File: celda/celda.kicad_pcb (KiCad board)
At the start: 4 copper layers, 119.6 x 48.1 mm, 87 parts, among them Q1 MMBT2222A, Q2 MMBT2222A, Q3 MMBT2222A, Q4 MMBT2222A, Q5 MMBT2222A, Q6 MMBT2222A, Q7 MMBT2222A, Q8 MMBT2222A, U1 LM339D, U10 BTS50010-1TAD, U11 BTS50010-1TAD, U2 74HC132D, U3 BTS50010-1TAD, U8 BTS50010-1TAD, U9 74HC132D

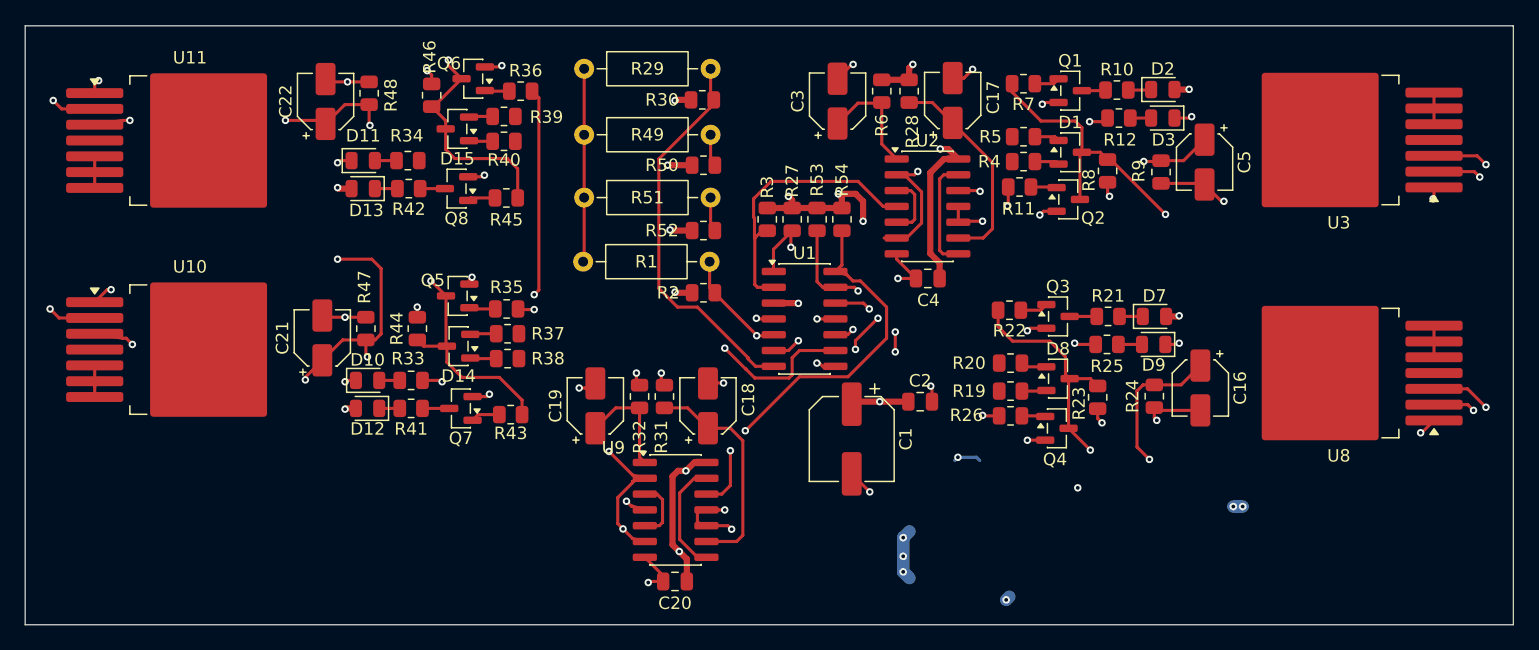
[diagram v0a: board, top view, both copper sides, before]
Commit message: Rediseña la celda dorada a doble cara y unifica el UUID raíz
Los componentes de control pasan a ambas caras (BTS y resistencias
THT DNP en F.Cu; LM339, 74HC132, transistores, BAT54C y la mayoría de
resistencias en B.Cu). La zona de huellas baja de 112,8 x 43,7 mm a
unos 82 x 35 mm (alrededor de un 41 % menos de área). Se cierran los
puentes de salida de los BTS y la red FALLA4.

El UUID de la hoja raíz, el del proyecto y las rutas de las huellas
quedan iguales, lo que elimina los 28 avisos de paridad del DRC.
El netlist es idéntico al anterior.

Pendiente en la celda: tiras de +12 V (7 conexiones abiertas), ajustar
el contorno Edge.Cuts al nuevo tamaño y la serigrafía de 0,7 mm.
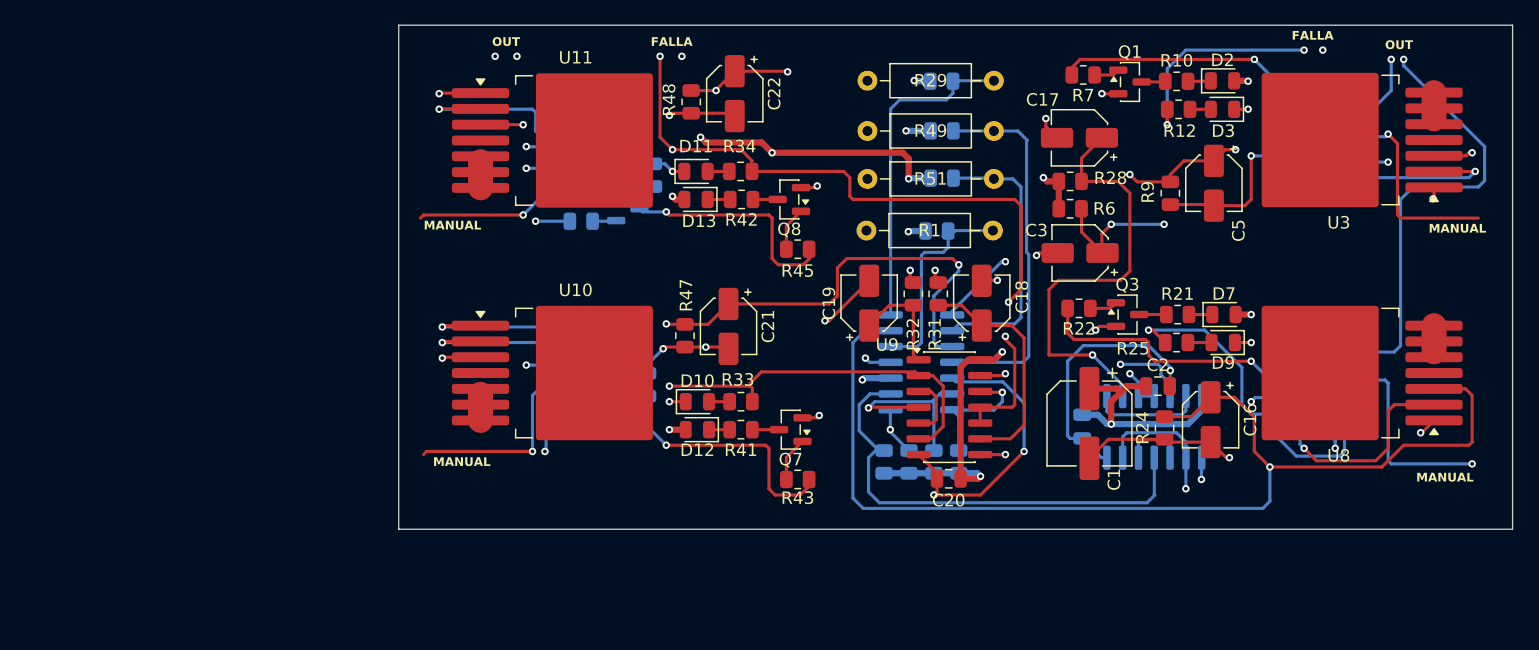
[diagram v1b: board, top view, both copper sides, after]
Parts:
- C4, D1, D14, D15, D8, Q2, Q4, Q5, Q6, R11, R19, R2, R20, R23, R26, R27, R3, R30, R35, R36, R37, R38, R39, R4, R40, R44, R46, R5, R50, R52, R53, R54, R8, U1, U2: moved to B.Cu
- moved C22 32.9 mm to (-110.5, 33.0), turned to -90 degrees
- moved C21 32.7 mm to (-111.0, 51.7), turned to -90 degrees
- moved U10 31.1 mm to (-123.3, 55.5)
- moved U11 31.0 mm to (-123.3, 36.8)
- moved R26 27.9 mm to (-60.4, 58.0), turned to 0 degrees
- moved R19 27.9 mm to (-60.4, 56.0), turned to 180 degrees
- moved R20 27.9 mm to (-60.4, 53.8), turned to 0 degrees
- moved R11 27.3 mm to (-60.3, 38.5), turned to 0 degrees
- moved D11 26.8 mm to (-113.6, 39.2)
- moved D13 26.8 mm to (-113.6, 41.5)
- moved Q8 26.8 mm to (-106.1, 41.5)
- moved R42 26.8 mm to (-110.0, 41.5)
- moved R34 26.8 mm to (-110.0, 39.2)
- moved R4 26.7 mm to (-60.7, 36.5), turned to 180 degrees
- moved R5 26.7 mm to (-60.7, 34.5), turned to 0 degrees
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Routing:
- net GND: track 86.6 -> 141.6 mm, vias 41 -> 27
- net /FALLA1: track 36.4 -> 90.5 mm, vias 3 -> 4
- net /ESP32_OUT3: track 0.00 -> 47.0 mm, vias 0 -> 2
- net /FALLA2: track 29.5 -> 72.2 mm
- net /FALLA3: track 35.9 -> 74.8 mm, vias 4 -> 3
- net Net-(U10-IS): track 96.6 -> 58.2 mm, vias 7 -> 3
- net /ESP32_OUT2: track 0.00 -> 34.3 mm, vias 0 -> 1
- net Net-(C3-Pad1): track 9.33 -> 36.3 mm, vias 0 -> 3
- net +3.3V: track 60.6 -> 86.0 mm, vias 19 -> 17
- net Net-(R53-Pad1): track 39.4 -> 15.3 mm, vias 4 -> 1
- net Net-(R54-Pad1): track 32.9 -> 10.4 mm, vias 2 -> 1
- net Net-(U1A--): track 88.7 -> 66.6 mm, vias 3 -> 4
- net /FALLA4: track 53.1 -> 74.7 mm, vias 3 -> 5
- net Net-(C17-Pad1): track 17.1 -> 34.9 mm, vias 0 -> 1
- net /ESP32_OUT4: track 0.00 -> 16.9 mm, vias 0 -> 2
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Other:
- board size 119.6 x 48.1 mm -> 89.5 x 40.5 mm
- board text added: "FALLA"
- board text added: "MANUAL"
- board text added: "OUT"
